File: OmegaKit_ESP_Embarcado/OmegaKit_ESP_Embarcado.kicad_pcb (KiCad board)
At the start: 2 copper layers, 76.5 x 36.5 mm, 57 parts, among them J13 Conn_01x02_Socket, J2 MOTOR_B, J5 MOTOR_A, Q25 QTR_1, Q26 QTR_2, SW1 TS-1088-AR02016, SW2 TS-1088-AR02016, SW3 SS-12D10G5, U2 TB6612FNG, U3 ESP32-WROOM-32, U5 AMS1117-3.3, U6 MP2307DN-HW-LF-P

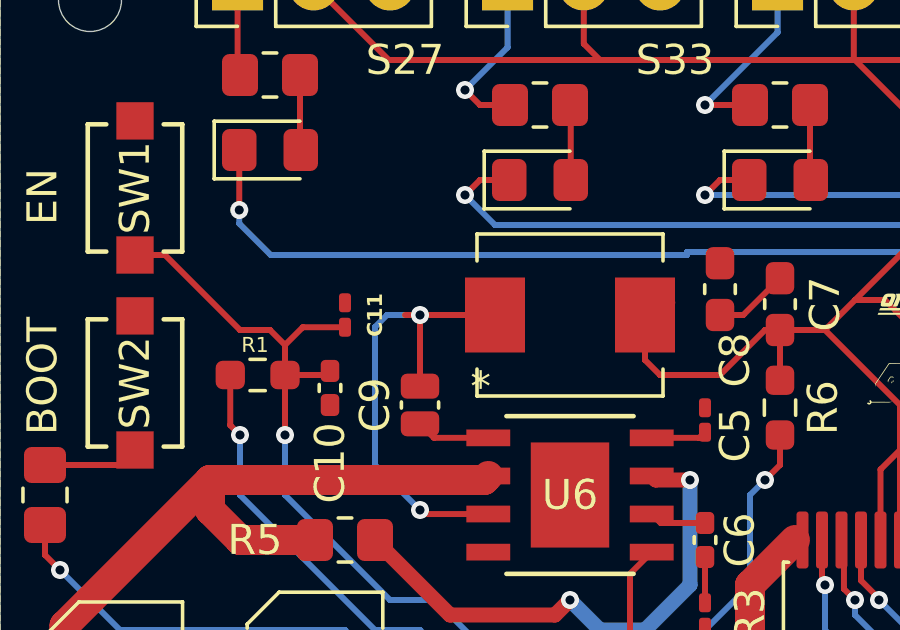
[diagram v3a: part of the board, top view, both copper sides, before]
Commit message: 🧹 chore(OmegaKit_ESP_Embarcado/*): Reorganiza projeto, plota projeto em PDF
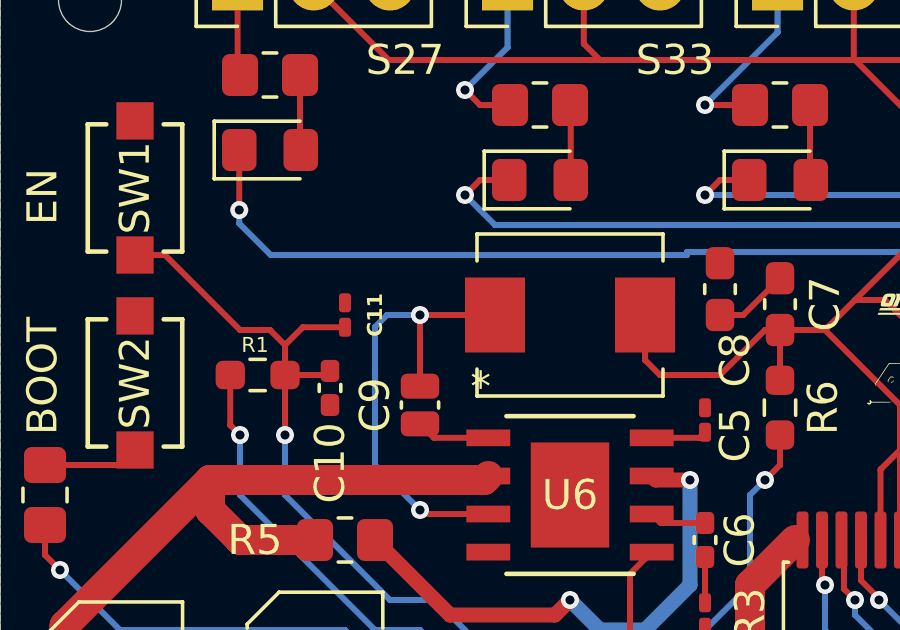
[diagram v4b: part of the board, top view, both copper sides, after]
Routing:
- net SW: track 16.1 -> 15.6 mm
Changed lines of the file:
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@@
+	)
+	(segment
+		(start 130.9 62.6)
+		(end 130.9 59.5)
+		(width 1)
+		(layer "F.Cu")
+		(net 13)
+	)
+	(segment
+		(start 104 57.5)
+		(end 99.15 62.35)
+		(width 1)
+		(layer "F.Cu")
+		(net 13)
+	)
+	(segment
+		(start 105 59.5)
+		(end 107.5 59.5)
+		(width 1)
+		(layer "F.Cu")
+		(net 13)
+	)
+	(segment
+		(start 122 63.5)
+		(end 119 66.5)
+		(width 1)
+		(layer "F.Cu")
+		(net 13)
+	)
+	(segment
+		(start 99.5 66)
+		(end 105.15 66)
+		(width 1)
+		(layer "F.Cu")
+		(net 13)
+	)
+	(segment
+		(start 109.801 71)
+		(end 109.801 67.801)
+		(width 1)
+		(layer "F.Cu")
+		(net 13)
+	)
+	(segment
+		(start 122 60.999)
+		(end 122 63.5)
+		(width 1)
+		(layer "F.Cu")
+		(net 13)
+	)
+	(segment
+		(start 109.801 67.801)
+		(end 108 66)
+		(width 1)
+		(layer "F.Cu")
+		(net 13)
+	)
+	(segment
+		(start 99.15 65.65)
+		(end 99.5 66)
+		(width 1)
+		(layer "F.Cu")
+		(net 13)
+	)
+	(segment
+		(start 130.5 63)
+		(end 130.9 62.6)
+		(width 1)
+		(layer "F.Cu")
+		(net 13)
+	)
+	(segment
+		(start 104 57.5)
+		(end 104 58.5)
+		(width 1)
+		(layer "F.Cu")
+		(net 13)
+	)
+	(segment
+		(start 108 66)
+		(end 105.15 66)
+		(width 1)
+		(layer "F.Cu")
+		(net 13)
+	)
+	(segment
+		(start 123.499 59.5)
+		(end 122 60.999)
+		(width 1)
+		(layer "F.Cu")
+		(net 13)
+	)
+	(segment
+		(start 99.15 62.35)
+		(end 99.15 63.825)
+		(width 1)
+		(layer "F.Cu")
+		(net 13)
+	)
+	(segment
+		(start 111.102 66.5)
+		(end 109.801 67.801)
+		(width 1)
+		(layer "F.Cu")
+		(net 13)
+	)
+	(segment
+		(start 116.5 71.5)
+		(end 116 71)
+		(width 1)
+		(layer "F.Cu")
+		(net 13)
+	)
+	(segment
+		(start 113.27585 57.365)
+		(end 113.14085 57.5)
+		(width 1)
+		(layer "F.Cu")
+		(net 13)
+	)
+	(segment
+		(start 119 66.5)
+		(end 111.102 66.5)
+		(width 1)
+		(layer "F.Cu")
+		(net 13)
+	)
+	(segment
+		(start 105.825 65.325)
+		(end 105.825 63.5)
+		(width 1)
+		(layer "F.Cu")
+		(net 13)
+	)
+	(segment
+		(start 122 63)
+		(end 130.5 63)
+		(width 1)
+		(layer "F.Cu")
+		(net 13)
+	)
+	(segment
+		(start 118.96 71.5)
+		(end 116.5 71.5)
+		(width 1)
+		(layer "F.Cu")
+		(net 13)
+	)
+	(segment
+		(start 104 58.5)
+		(end 105 59.5)
+		(width 1)
+		(layer "F.Cu")
+		(net 13)
+	)
+	(segment
+		(start 113.14085 57.5)
+		(end 104 57.5)
+		(width 1)
+		(layer "F.Cu")
+		(net 13)
+	)
+	(segment
+		(start 116 71)
+		(end 114.5 71)
+		(width 1)
+		(layer "F.Cu")
+		(net 13)
 	)
 	(segment
@@
 	)
 	(segment
-		(start 130.9 62.6)
-		(end 130.9 59.5)
-		(width 1)
-		(layer "F.Cu")
-		(net 13)
-	)
-	(segment
-		(start 104 57.5)
-		(end 99.15 62.35)
-		(width 1)
-		(layer "F.Cu")
-		(net 13)
-	)
-	(segment
-		(start 105 59.5)
-		(end 107.5 59.5)
-		(width 1)
-		(layer "F.Cu")
-		(net 13)
-	)
-	(segment
-		(start 122 63.5)
-		(end 119 66.5)
-		(width 1)
-		(layer "F.Cu")
-		(net 13)
-	)
-	(segment
-		(start 99.5 66)
-		(end 105.15 66)
-		(width 1)
-		(layer "F.Cu")
-		(net 13)
-	)
-	(segment
-		(start 109.801 71)
-		(end 109.801 67.801)
-		(width 1)
-		(layer "F.Cu")
-		(net 13)
-	)
-	(segment
-		(start 122 60.999)
-		(end 122 63.5)
-		(width 1)
-		(layer "F.Cu")
-		(net 13)
-	)
-	(segment
-		(start 109.801 67.801)
-		(end 108 66)
-		(width 1)
-		(layer "F.Cu")
-		(net 13)
-	)
-	(segment
-		(start 99.15 65.65)
-		(end 99.5 66)
-		(width 1)
-		(layer "F.Cu")
-		(net 13)
-	)
-	(segment
-		(start 130.5 63)
-		(end 130.9 62.6)
-		(width 1)
-		(layer "F.Cu")
-		(net 13)
-	)
-	(segment
-		(start 104 57.5)
-		(end 104 58.5)
-		(width 1)
-		(layer "F.Cu")
-		(net 13)
-	)
-	(segment
-		(start 108 66)
-		(end 105.15 66)
-		(width 1)
-		(layer "F.Cu")
-		(net 13)
-	)
-	(segment
-		(start 123.499 59.5)
-		(end 122 60.999)
-		(width 1)
-		(layer "F.Cu")
-		(net 13)
-	)
-	(segment
-		(start 99.15 62.35)
-		(end 99.15 63.825)
-		(width 1)
-		(layer "F.Cu")
-		(net 13)
-	)
-	(segment
-		(start 111.102 66.5)
-		(end 109.801 67.801)
-		(width 1)
-		(layer "F.Cu")
-		(net 13)
-	)
-	(segment
-		(start 116.5 71.5)
-		(end 116 71)
-		(width 1)
-		(layer "F.Cu")
-		(net 13)
-	)
-	(segment
-		(start 113.27585 57.365)
-		(end 113.14085 57.5)
-		(width 1)
-		(layer "F.Cu")
-		(net 13)
-	)
-	(segment
-		(start 119 66.5)
-		(end 111.102 66.5)
-		(width 1)
-		(layer "F.Cu")
-		(net 13)
-	)
-	(segment
-		(start 122 63)
-		(end 130.5 63)
-		(width 1)
-		(layer "F.Cu")
-		(net 13)
-	)
-	(segment
-		(start 118.96 71.5)
-		(end 116.5 71.5)
-		(width 1)
-		(layer "F.Cu")
-		(net 13)
-	)
-	(segment
-		(start 104 58.5)
-		(end 105 59.5)
-		(width 1)
-		(layer "F.Cu")
-		(net 13)
-	)
-	(segment
-		(start 113.14085 57.5)
-		(end 104 57.5)
-		(width 1)
-		(layer "F.Cu")
-		(net 13)
-	)
-	(segment
-		(start 105.825 65.325)
-		(end 105.825 63.5)
-		(width 1)
-		(layer "F.Cu")
-		(net 13)
-	)
-	(segment
-		(start 116 71)
-		(end 114.5 71)
-		(width 1)
-		(layer "F.Cu")
-		(net 13)
-	)
-	(segment
 		(start 163 62.5)
 		(end 163.3325 62.8325)
@@
 	)
 	(segment
-		(start 110.5 52)
+		(start 111 52)
 		(end 113.5 52)
 		(width 0.2)

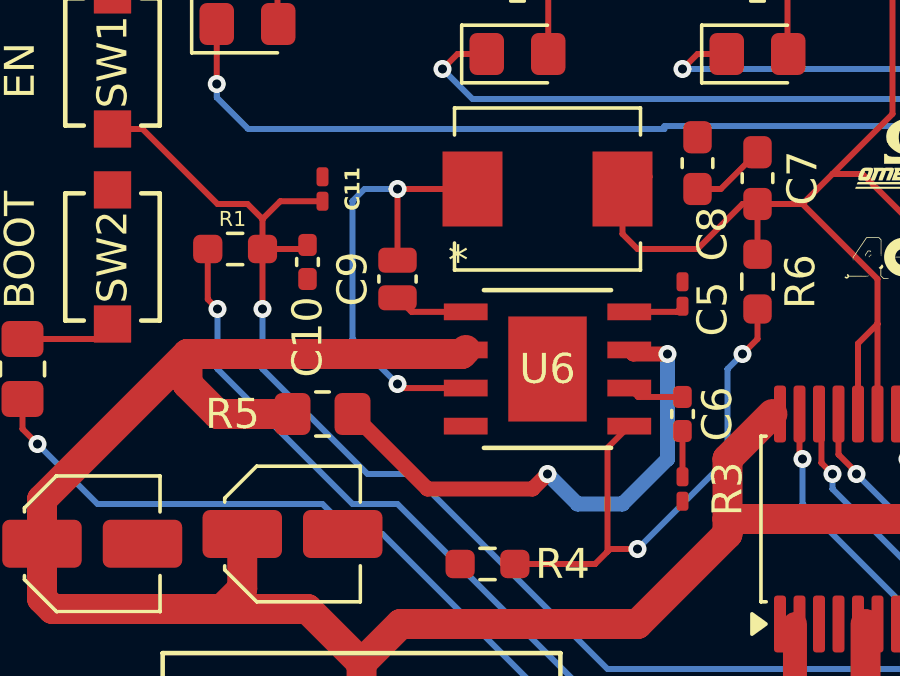
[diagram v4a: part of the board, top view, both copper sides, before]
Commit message: ✨ feat: Pequenas revisões no esquemático de OmegaKit_ESP_Embarcado/, criação de OmegaKit_ESP_Embarcado_Simplificado/
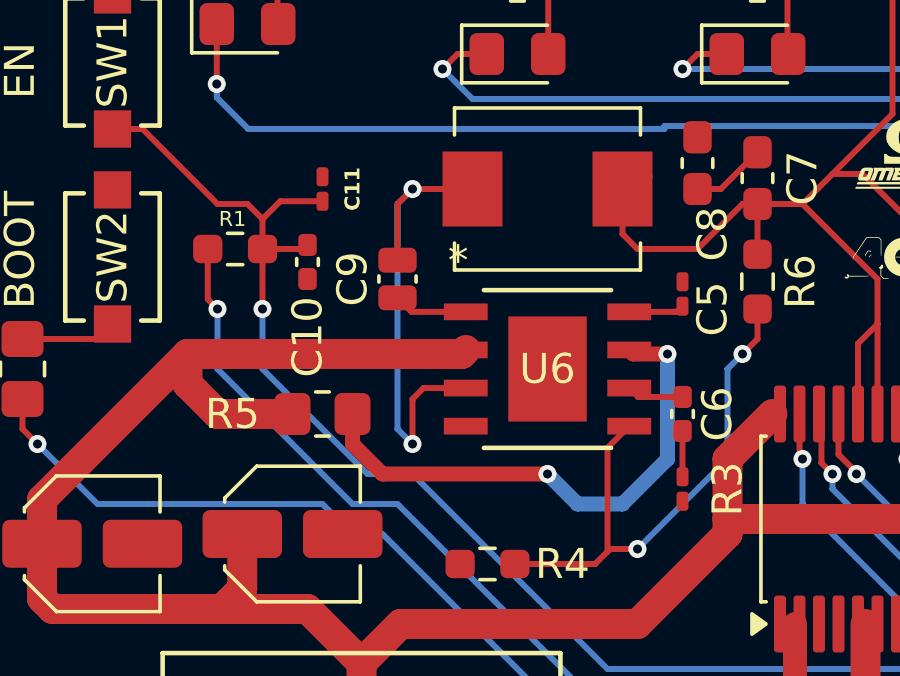
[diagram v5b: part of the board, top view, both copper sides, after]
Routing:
- net SW: track 15.6 -> 16.9 mm
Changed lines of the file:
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@@
 	)
 	(segment
-		(start 111 52)
+		(start 111.5 52)
 		(end 113.5 52)
 		(width 0.2)
@@
 	(segment
 		(start 111 54.3725)
-		(end 111 52)
-		(width 0.2)
-		(layer "F.Cu")
-		(net 49)
-	)
-	(segment
-		(start 111.135 58.635)
-		(end 111 58.5)
-		(width 0.2)
-		(layer "F.Cu")
-		(net 49)
-	)
-	(segment
-		(start 113.27585 58.635)
-		(end 111.135 58.635)
-		(width 0.2)
-		(layer "F.Cu")
-		(net 49)
-	)
-	(via
-		(at 111 52)
-		(size 0.6)
-		(drill 0.3)
-		(layers "F.Cu" "B.Cu")
-		(net 49)
-	)
-	(via
-		(at 111 58.5)
-		(size 0.6)
-		(drill 0.3)
-		(layers "F.Cu" "B.Cu")
-		(net 49)
-	)
-	(segment
-		(start 109.901 52)
-		(end 109.5 52.401)
-		(width 0.2)
-		(layer "B.Cu")
-		(net 49)
-	)
-	(segment
-		(start 109.5 52.401)
-		(end 109.5 57)
-		(width 0.2)
-		(layer "B.Cu")
-		(net 49)
-	)
-	(segment
-		(start 111 52)
-		(end 109.901 52)
-		(width 0.2)
-		(layer "B.Cu")
-		(net 49)
-	)
-	(segment
-		(start 109.5 57)
-		(end 111 58.5)
+		(end 111 52.5)
+		(width 0.2)
+		(layer "F.Cu")
+		(net 49)
+	)
+	(segment
+		(start 111.5 60.5)
+		(end 111.5 59)
+		(width 0.2)
+		(layer "F.Cu")
+		(net 49)
+	)
+	(segment
+		(start 111.865 58.635)
+		(end 113.27585 58.635)
+		(width 0.2)
+		(layer "F.Cu")
+		(net 49)
+	)
+	(segment
+		(start 111.5 59)
+		(end 111.865 58.635)
+		(width 0.2)
+		(layer "F.Cu")
+		(net 49)
+	)
+	(segment
+		(start 111 52.5)
+		(end 111.5 52)
+		(width 0.2)
+		(layer "F.Cu")
+		(net 49)
+	)
+	(via
+		(at 111.5 52)
+		(size 0.6)
+		(drill 0.3)
+		(layers "F.Cu" "B.Cu")
+		(net 49)
+	)
+	(via
+		(at 111.5 60.5)
+		(size 0.6)
+		(drill 0.3)
+		(layers "F.Cu" "B.Cu")
+		(net 49)
+	)
+	(segment
+		(start 111 52.5)
+		(end 111 60)
+		(width 0.2)
+		(layer "B.Cu")
+		(net 49)
+	)
+	(segment
+		(start 111.5 52)
+		(end 111 52.5)
+		(width 0.2)
+		(layer "B.Cu")
+		(net 49)
+	)
+	(segment
+		(start 111 60)
+		(end 111.5 60.5)
 		(width 0.2)
 		(layer "B.Cu")
@@
 	)
 	(segment
-		(start 116 61.5)
-		(end 115.5 62)
-		(width 0.5)
-		(layer "F.Cu")
-		(net 51)
-	)
-	(segment
 		(start 118.85915 57.5)
 		(end 118.72415 57.365)
@@
 	)
 	(segment
+		(start 110.5 61.5)
+		(end 109.5 60.5)
+		(width 0.5)
+		(layer "F.Cu")
+		(net 51)
+	)
+	(segment
 		(start 120 57.5)
 		(end 118.85915 57.5)
@@
 	)
 	(segment
-		(start 115.5 62)
-		(end 112 62)
-		(width 0.5)
-		(layer "F.Cu")
-		(net 51)
-	)
-	(segment
-		(start 112 62)
+		(start 116 61.5)
+		(end 110.5 61.5)
+		(width 0.5)
+		(layer "F.Cu")
+		(net 51)
+	)
+	(segment
+		(start 109.5 60.5)
 		(end 109.5 59.5)
 		(width 0.5)
